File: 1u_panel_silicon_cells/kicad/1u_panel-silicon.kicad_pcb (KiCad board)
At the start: 2 copper layers, 83 x 100 mm, 147 parts, among them J1 MMS-104-01-[F/L]-SH, J2 2-1734592-0, Q1 DMP3050LVT-7, Q2 DMP2240UDM-7, U1 TCAN330GDCNT, U10 TPS63060DSCR, U11 TMP101NA/3KSLOTTED, U12 LTC4412, U13 LTC4411, U14 LTC4411, U15 LTC4411, U16 LTC4411, U2 TMP101NA/3KSLOTTED, U3 LT1618EMSTRPBF, U4 INA226, U5 LTC4411, U6 LTC4411, U7 STM32F091CCT7, U8 LTC4411, U9 LTC4411, X1 ECS-160-10-36Q-ES-TR

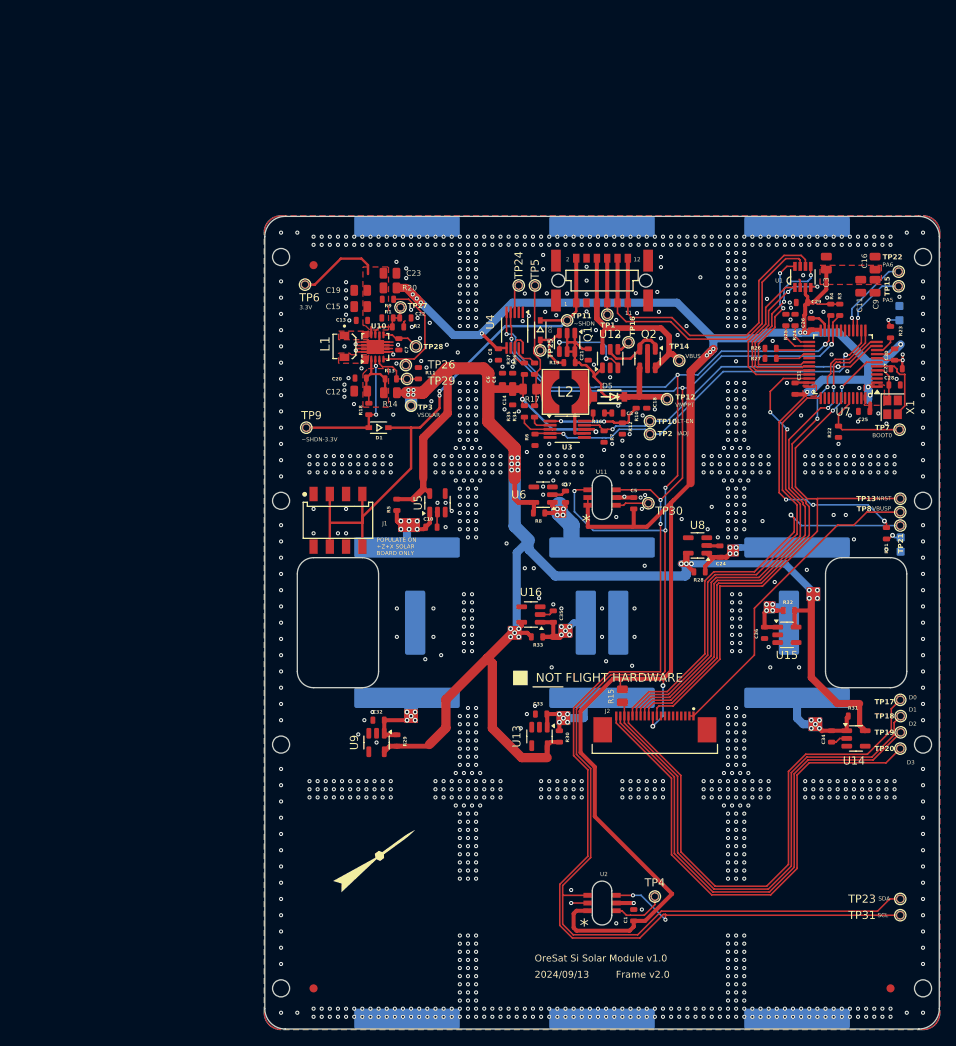
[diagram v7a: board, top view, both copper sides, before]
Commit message: Polish on Jack's final design. Swapped out rectangles for zones on multiple layers, cleaned up a lot of small layout bits, fixed some mechanical crashes with screw heads, fixed up the silk screen, and added 3D models.
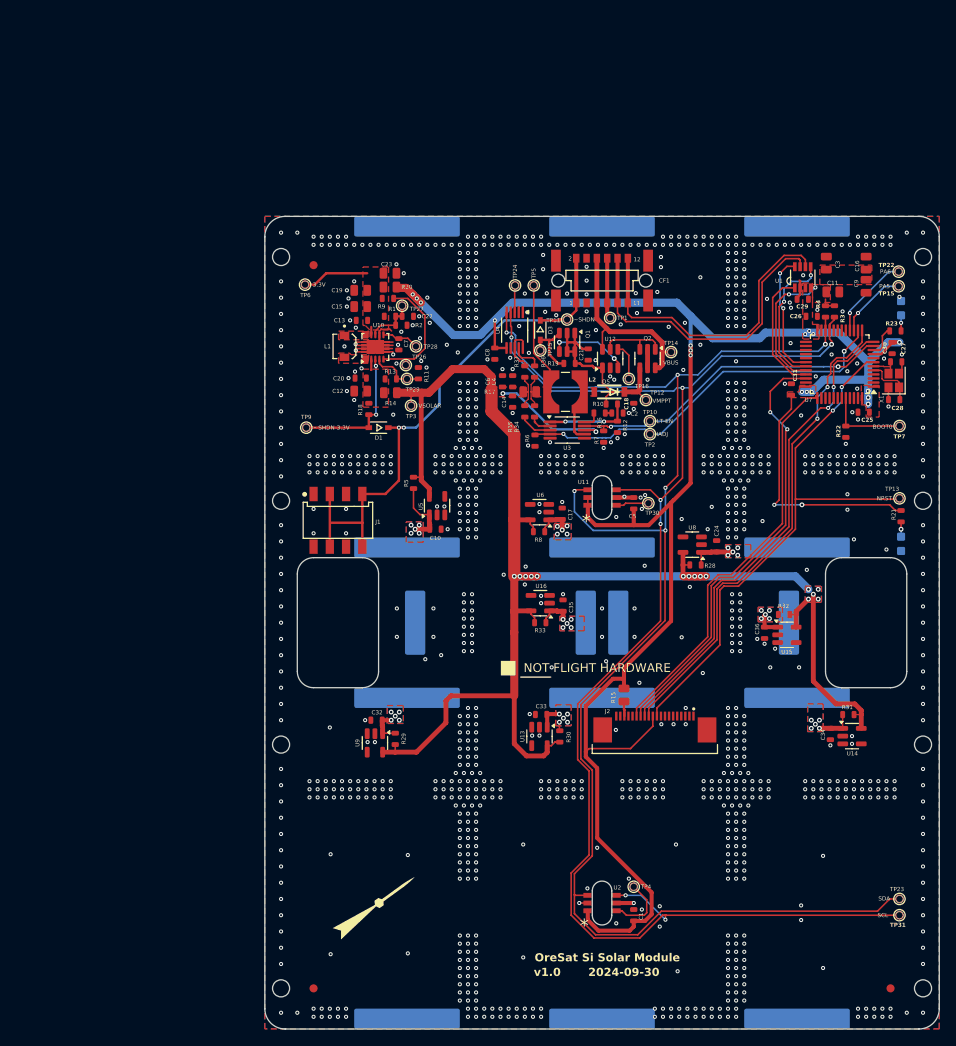
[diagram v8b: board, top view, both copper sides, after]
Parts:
- removed R24, R25, R26, R27: 1k/NP, oresat-passives:0603-C-NOSILK
- removed TP17, TP18, TP19, TP20, TP21, TP8: TEST-POINT-LARGE-SQUARE, oresat-misc:TestPoint-0.75mm-th
- moved LOGO1 5.80 mm to (120.7, 139.8)
- moved TP16 4.50 mm to (151.8, 75.0)
- moved C11 3.50 mm to (176.9, 64.3), turned to 0 degrees
- moved R5 3.39 mm to (125.3, 87.8)
- moved X1 3.30 mm to (184.4, 75.2), turned to 90 degrees
- moved R10 3.01 mm to (149.7, 78.1), turned to 180 degrees
- moved TP4 2.87 mm to (152.4, 137.5)
- moved R21 2.77 mm to (185.3, 91.9)
- moved TP12 2.60 mm to (153.9, 77.6)
- moved R8 2.30 mm to (140.8, 93.8)
- moved U6 2.20 mm to (140.8, 91.4)
- moved C17 2.14 mm to (143.6, 91.6)
- moved U$1 1.92 mm to (136.3, 111.2)
- moved U16 1.81 mm to (140.9, 102.6)
- moved C35 1.81 mm to (143.7, 102.9)
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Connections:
- J2 pad 1: Net-(J2-VBUSP-Pad1) -> unconnected-(J2-VBUSP-Pad1)_1
- J2 pad 16: Net-(J2-SWO) -> unconnected-(J2-SWO-Pad16)
- J2 pad 17: Net-(J2-DEBUG-0) -> unconnected-(J2-DEBUG-0-Pad17)
- J2 pad 19: Net-(J2-DEBUG-2) -> unconnected-(J2-DEBUG-2-Pad19)
- J2 pad 2: Net-(J2-VBUSP-Pad1) -> unconnected-(J2-VBUSP-Pad1)
- J2 pad 20: Net-(J2-DEBUG-3) -> unconnected-(J2-DEBUG-3-Pad20)
- U7 pad 25: /1u_panel-microcontroller/SMSN0 -> unconnected-(U7-PB12-Pad25)
- U7 pad 26: /1u_panel-microcontroller/SMSN1 -> unconnected-(U7-PB13-Pad26)
- U7 pad 27: /1u_panel-microcontroller/SMSN2 -> unconnected-(U7-PB14-Pad27)
- U7 pad 28: /1u_panel-microcontroller/SMSN3 -> unconnected-(U7-PB15-Pad28)
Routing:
- net Net-(J2-DEBUG-0): track 65.9 -> 0.00 mm
- net Net-(J2-DEBUG-1): track 66.7 -> 1.80 mm
- net Net-(J2-DEBUG-2): track 64.4 -> 0.00 mm
- net Net-(J2-DEBUG-3): track 64.3 -> 0.00 mm
- net Net-(J2-SWO): track 51.4 -> 0.00 mm, vias 1 -> 0
- net Net-(J2-VBUSP-Pad1): track 39.7 -> 0.00 mm
- net 3.3V: track 272.9 -> 249.6 mm
- net VSOLAR: track 226.1 -> 203.3 mm, vias 24 -> 17
- net GND: track 35.2 -> 21.3 mm, vias 1221 -> 1118
- net SDA: track 193.5 -> 184.9 mm
- net Net-(D10-A1): track 12.8 -> 4.20 mm
- net Net-(D8-A1): track 13.7 -> 5.45 mm, vias 4 -> 5
- net Net-(U10-VIN): track 9.56 -> 1.85 mm
- net SCL: track 187.7 -> 180.7 mm
- net Net-(D11-A1): track 11.1 -> 4.77 mm
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- added copper zone on B.Cu, net Net-(D10-A1)
- added copper zone on F.Cu, net Net-(D10-A1)
- added copper zone on B.Cu, net Net-(D11-A1)
- added copper zone on F.Cu, net Net-(D11-A1)
- added copper zone on B.Cu, net Net-(D12-A1)
- added copper zone on F.Cu, net Net-(D12-A1)
- added copper zone on B.Cu, net Net-(D13-A1)
- added copper zone on F.Cu, net Net-(D13-A1)
- added copper zone on B.Cu, net Net-(D2-A1)
- added copper zone on F.Cu, net Net-(D2-A1)
- added copper zone on F.Cu, net Net-(D5-ANODE)
- added copper zone on B.Cu, net Net-(D7-A1)
- added copper zone on F.Cu, net Net-(D7-A1)
- added copper zone on B.Cu, net Net-(D8-A1)
- added copper zone on F.Cu, net Net-(D8-A1)
- added copper zone on B.Cu, net Net-(D9-A1)
- added copper zone on F.Cu, net Net-(D9-A1)
- added copper zone on F.Cu, net Net-(L2-Pad1)
- added copper zone on B.Cu, net VSOLAR
- added copper zone on F.Cu, net VSOLAR
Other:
- board text added: "${ISSUE_DATE}"
- board text added: "CAUTION! No component may be >= 2.0 mm on the front side due to frame height."
- board text added: "CAUTION! See User.Draiwings for components < 0.7 mm height in circles"
- board text added: "OreSat Si Solar Module"
- board text added: "v${REVISION}"
- board text removed: "D0"
- board text removed: "D1"
- board text removed: "D2"
- board text removed: "D3"
- board text removed: "NOTE: See User.Draiwings layer for component placement restrictions -> <0.7mm component height in circles"
- board text removed: "OreSat Si Solar Module v1.0"
- board text removed: "POPULATE ON +Z+X SOLAR BOARD ONLY"
- board text removed: "SWO"
- board text removed: "VBUSP"
